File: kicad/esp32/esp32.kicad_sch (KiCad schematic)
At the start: 27 parts, among them J101 RJ45, J102 NodeMCU, J103 Annunciator, U101 74LS14, X101 Mouse Bites, X102 Mouse Bites, X103 Mouse Bites, X104 Mouse Bites

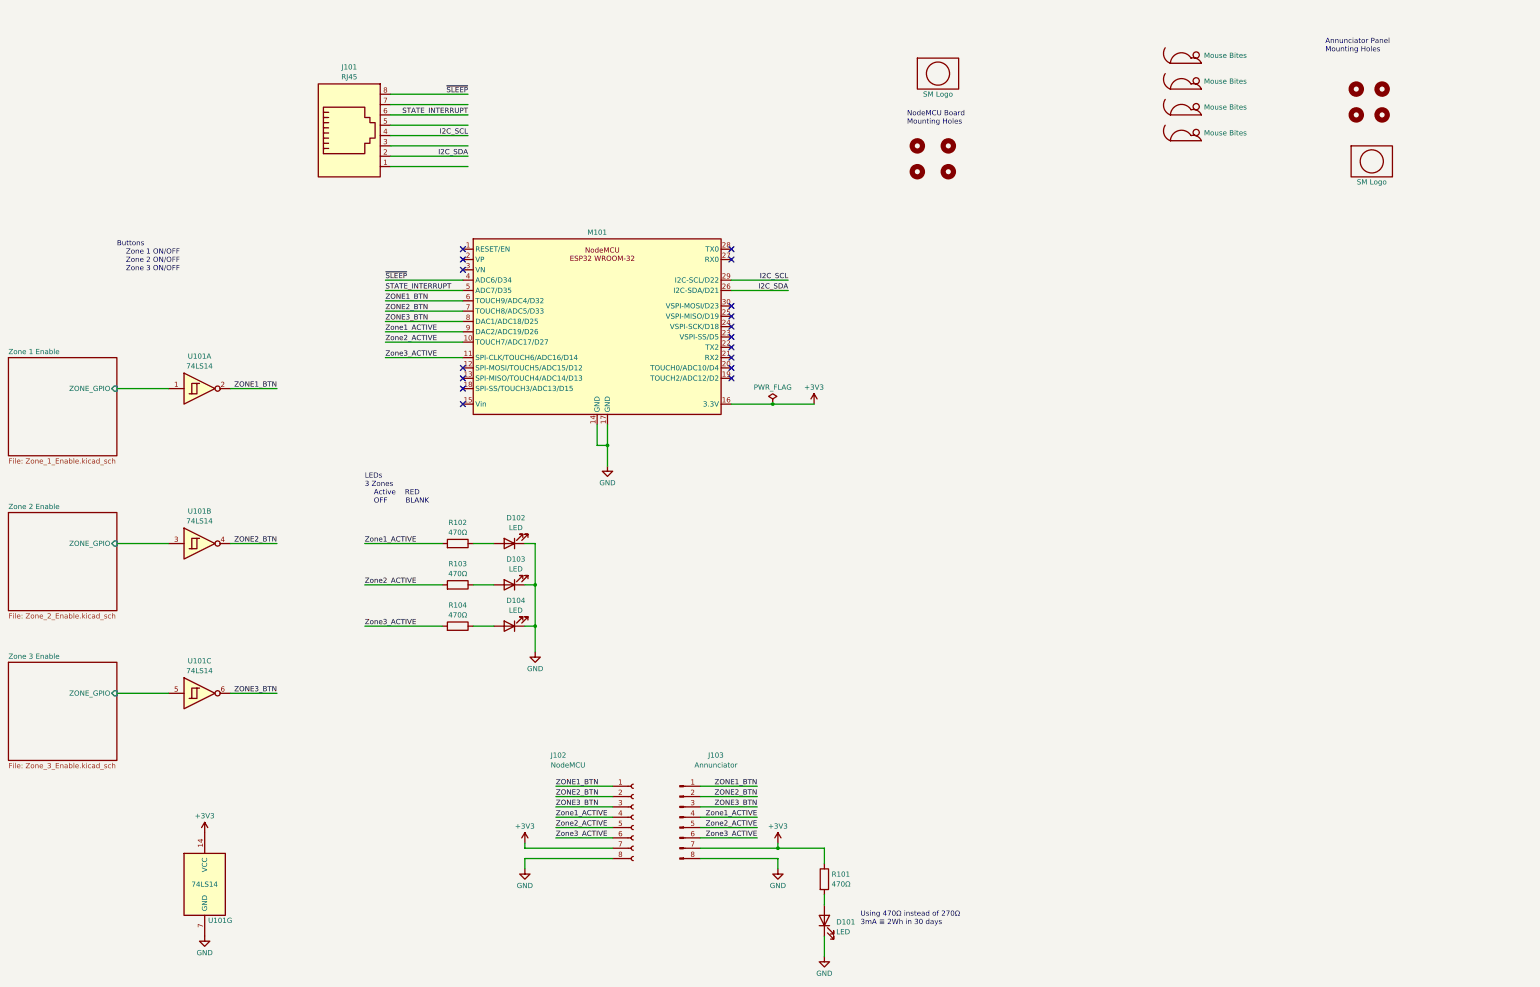
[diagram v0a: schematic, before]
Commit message: Created the front panel artwork with drill marks
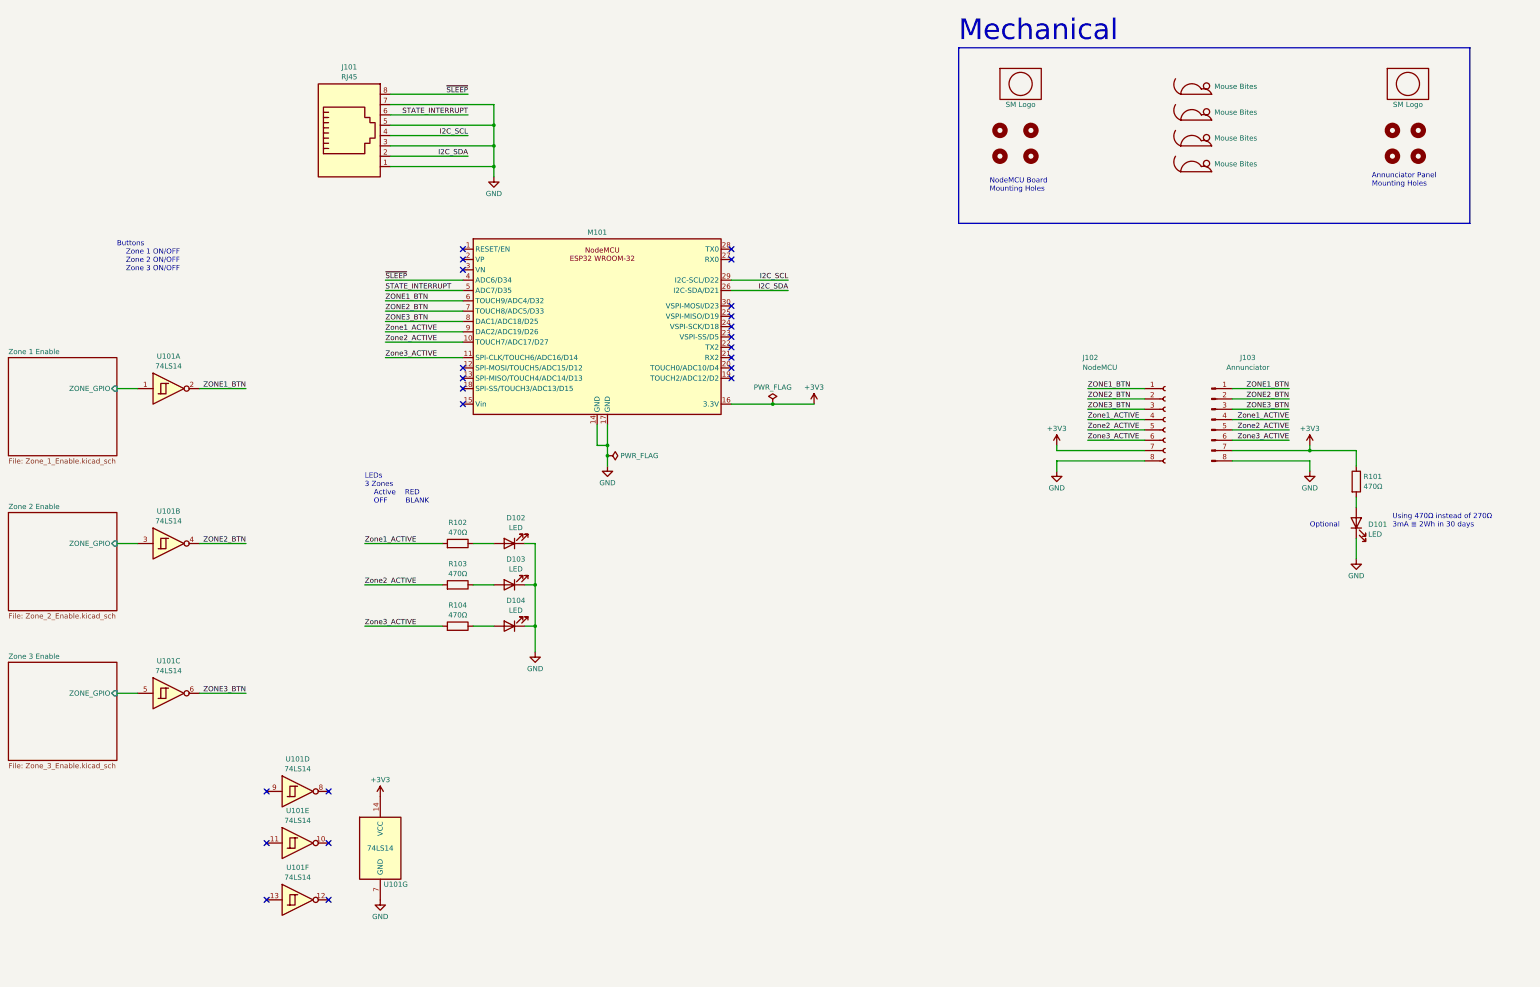
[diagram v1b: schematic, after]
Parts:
- added unit 5 of U101
- added unit 6 of U101
- added unit 4 of U101
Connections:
- net GND: now also J101.1, J101.3, J101.5, J101.7
- no-connect marks 17 -> 23
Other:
- note added: "Mechanical"
- note added: "Optional"
- moved on the sheet: D101, J102, J103, R101, U101A, U101B, U101C, U101G

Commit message: Added some comments
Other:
- note added: "Hardware debounce to save some CPU cycles."
- note added: "Power will come from the Mini USB for this system"
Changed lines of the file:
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@@
+    (effects (font (size 1.27 1.27)) (justify left bottom))
+  )
+  (text "Power will come from the \nMini USB for this system"
+    (at 115.57 119.38 0)
     (effects (font (size 1.27 1.27)) (justify left bottom))
   )
@@
     (effects (font (size 1.27 1.27)) (justify left bottom))
   )
+  (text "Hardware debounce \nto save some CPU cycles." (at 30.48 100.33 0)
+    (effects (font (size 1.27 1.27)) (justify left bottom))
+  )

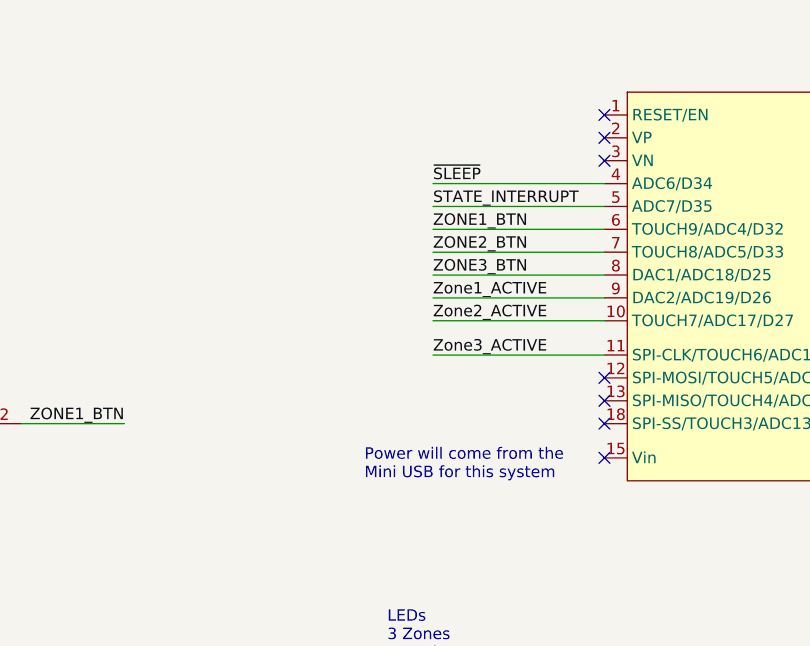
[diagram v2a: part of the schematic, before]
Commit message: Pin reassignments after starting the firmware
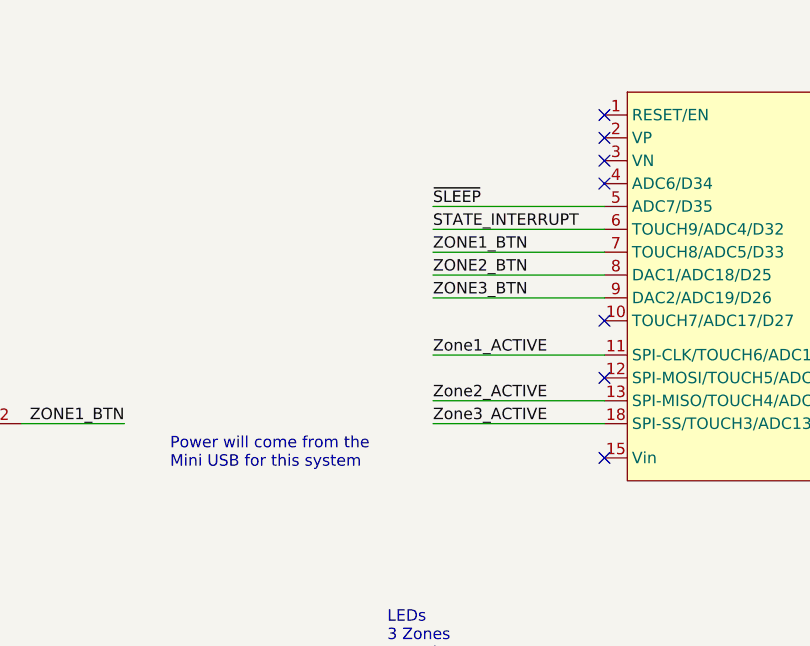
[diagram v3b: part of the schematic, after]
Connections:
- net STATE_INTERRUPT: now also M101.6 (TOUCH9/ADC4/D32); no longer M101.5 (ADC7/D35)
- net ZONE1_BTN: now also M101.7 (TOUCH8/ADC5/D33); no longer M101.6 (TOUCH9/ADC4/D32)
- net ZONE2_BTN: now also M101.8 (DAC1/ADC18/D25); no longer M101.7 (TOUCH8/ADC5/D33)
- net ZONE3_BTN: now also M101.9 (DAC2/ADC19/D26); no longer M101.8 (DAC1/ADC18/D25)
- net Zone1_ACTIVE: now also M101.11 (SPI-CLK/TOUCH6/ADC16/D14); no longer M101.9 (DAC2/ADC19/D26)
- net Zone2_ACTIVE: now also M101.13 (SPI-MISO/TOUCH4/ADC14/D13); no longer M101.10 (TOUCH7/ADC17/D27)
- net Zone3_ACTIVE: now also M101.18 (SPI-SS/TOUCH3/ADC13/D15); no longer M101.11 (SPI-CLK/TOUCH6/ADC16/D14)
- net ~{SLEEP}: now also M101.5 (ADC7/D35); no longer M101.4 (ADC6/D34)

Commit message: Completed the release for OSH Park
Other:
- note added: "D12 Must be low during boot"
- note added: "D34 Input only"
- note added: "OUTPUT #define TL2C_SLEEP 35 #define TL2C_RELAY_INT 32 #define TL2C_ZONE1_ACTIVE 14 #define TL2C_ZONE2_ACTIVE 13 #define TL2C_ZONE3_ACTIVE 15 INPUT #define TL2C_ZONE1_BUTTON 33 #define TL2C_ZONE2_BUTTON 25 #define TL2C_ZONE3_BUTTON 26"

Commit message: Created rev 1.01 - Addes some more labels and annotations
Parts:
- added Lg103: SM Logo, sjm-mechanical:MyBasic_rounded_50_1_USER5, symbol sjm-mechanical:logo
- added Lg104, Lg105: Non-TCP, sjm-mechanical:Non_TCP, symbol sjm-mechanical:logo
- added Lg106, Lg107: SM Logo, sjm-mechanical:MyBasic_rounded_50_1, symbol sjm-mechanical:logo

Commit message: changes to help with the writeup
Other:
- note removed: "Buttons Zone 1 ON/OFF Zone 2 ON/OFF Zone 3 ON/OFF"
- note removed: "D12 Must be low during boot"
- note removed: "D34 Input only"
- moved on the sheet: D101, D102, D103, D104, J101, J102, J103, R101, R102, R103, R104
